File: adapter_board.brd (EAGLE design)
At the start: 40 x 40 mm, 29 parts, among them IC1 LT8336HV#PBF, J1 62684-401100AHLF, J2 SFV6R-3STE1HLF, J3 54548-2271

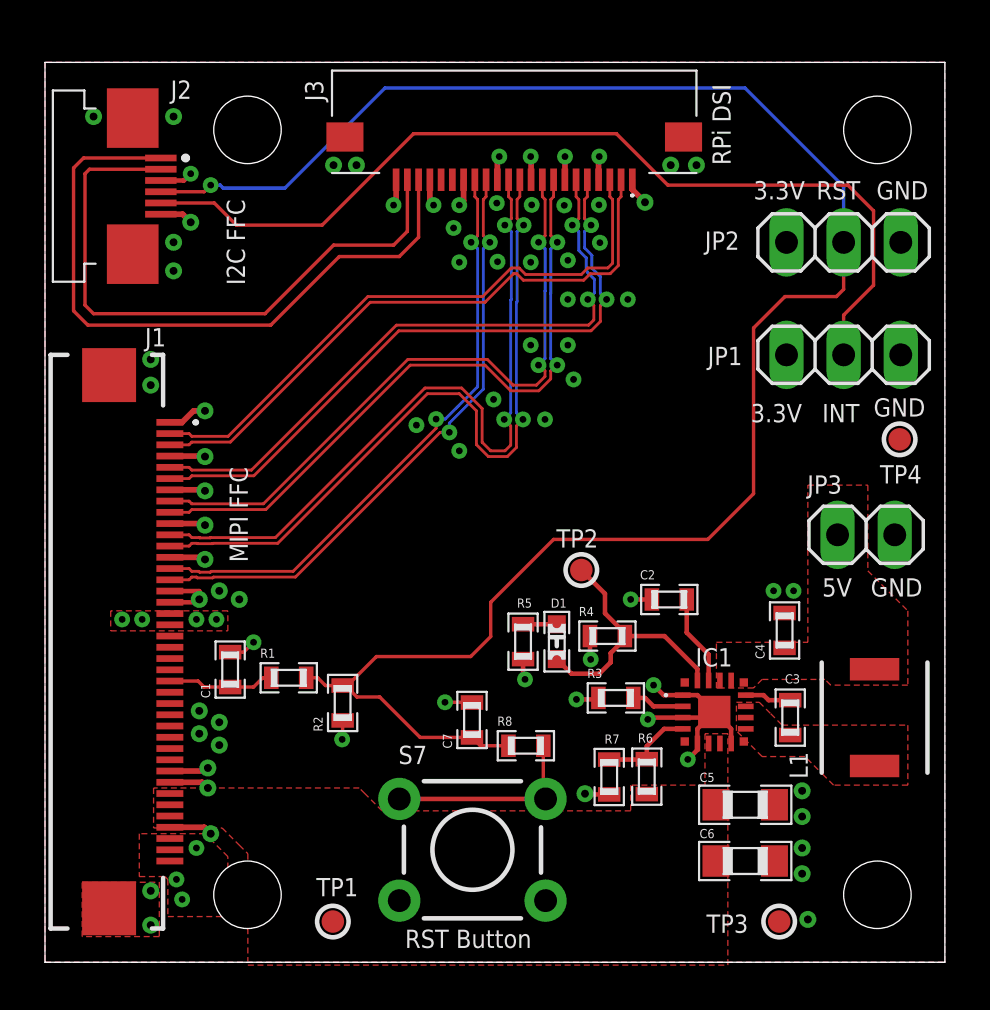
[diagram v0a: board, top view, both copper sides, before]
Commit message: Changed inductor L1.
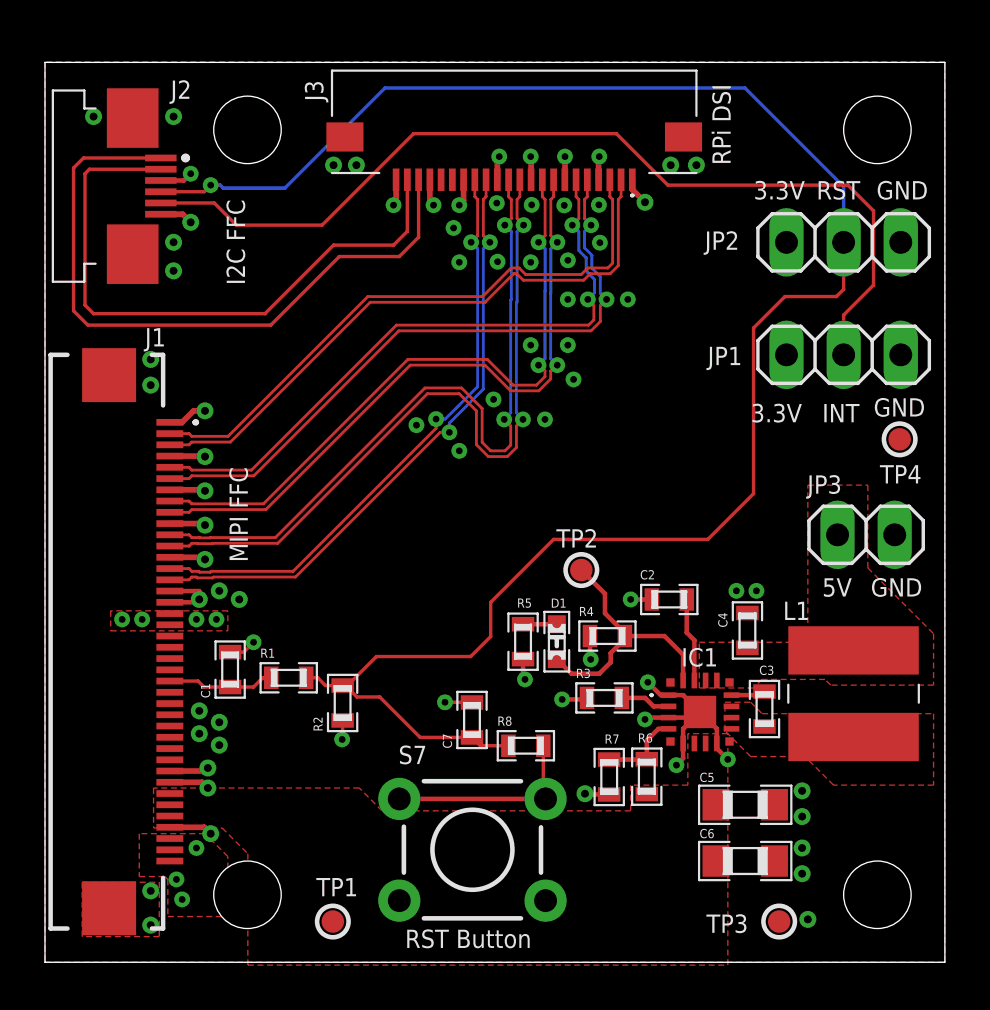
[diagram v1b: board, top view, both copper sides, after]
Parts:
- L1: value 1235AS-H-2R4M=P3 -> SDR0603-2R5ML; device SamacSys_Parts:1235ASH100MP3 -> SamacSys_Parts:SDR06032R5ML
- moved C4 1.65 mm to (31.2, 14.8)
- moved L1 1.42 mm to (35.9, 11.9), turned to 0 degrees
- moved C3 1.20 mm to (32.0, 11.3)
- moved IC1 0.64 mm to (29.1, 11.1)
- moved R3 0.51 mm to (24.9, 11.8)
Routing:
- net N$7: track 2.07 -> 1.53 mm
- net VSS: track 42.1 -> 42.5 mm, vias 69 -> 70

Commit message: Changed min width/spacing to 6/6. Length matched DSI traces.
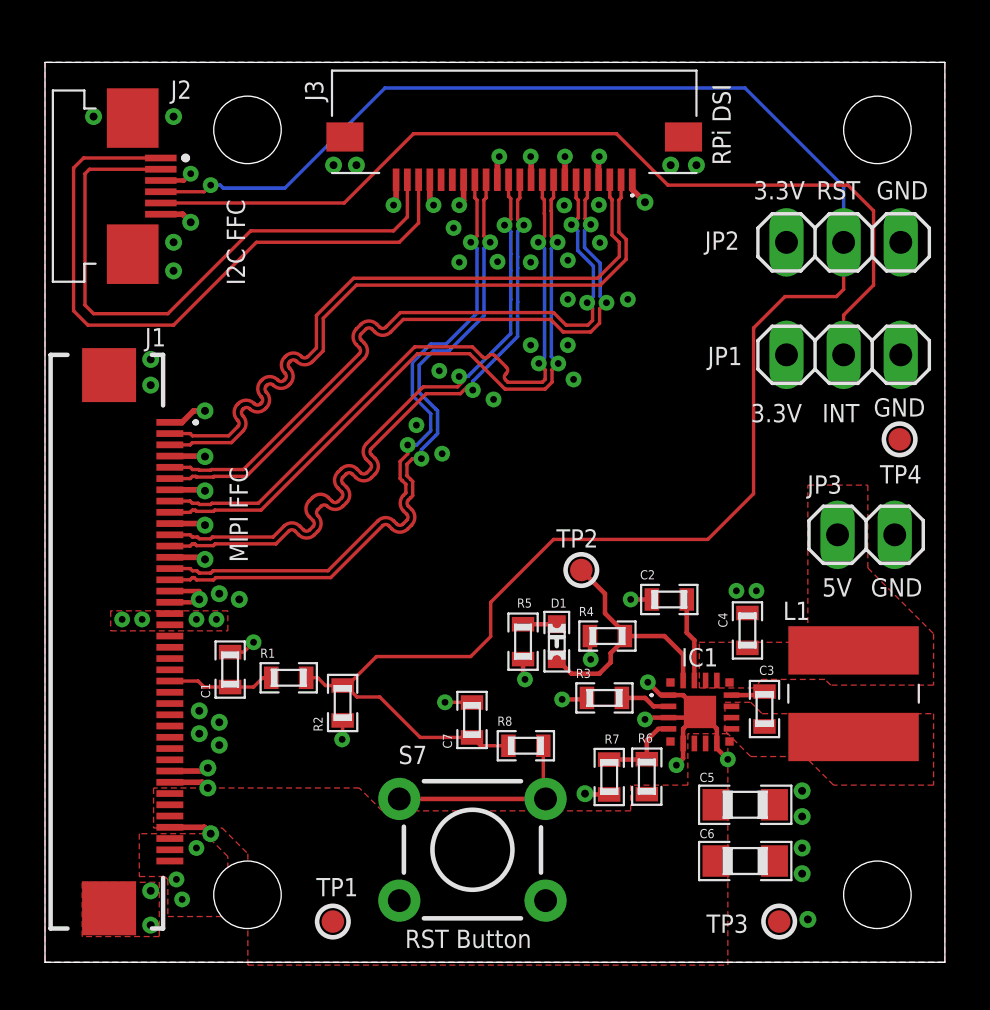
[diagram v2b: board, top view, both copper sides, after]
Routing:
- net DSI_D2_N: track 32.9 -> 29.6 mm
- net DSI_D3_N: track 27.3 -> 30.5 mm
- net DSI_D3_P: track 26.9 -> 30.0 mm
- net DSI_D2_P: track 32.5 -> 29.6 mm
- net DSI_D0_P: track 26.9 -> 29.6 mm
- net DSI_D0_N: track 27.3 -> 30.0 mm
- net DSI_D1_N: track 29.1 -> 30.6 mm
- net DSI_D1_P: track 28.7 -> 30.0 mm
- net DSI_CLK_P: track 29.3 -> 30.1 mm
- net !INT: track 42.1 -> 41.3 mm
- net DSI_CLK_N: track 29.7 -> 30.3 mm
- net VSS: vias 70 -> 68

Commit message: Changed PGOOD LED to 5V rail.
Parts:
- D1: value Red -> Green
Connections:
- net VCC_3V3: no longer R4.1, R5.2
- net VCC_5V0: now also R4.1, R5.2
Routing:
- net VCC_5V0: track 0.00 -> 14.8 mm, vias 0 -> 3
- net VCC_3V3: track 5.47 -> 3.48 mm, vias 12 -> 10
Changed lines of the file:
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@@
 <grid distance="5" unitdist="mil" unit="mil" style="dots" multiple="1" display="yes" altdistance="0.000123031496" altunitdist="mil" altunit="mil"/>
 <layers>
-<layer number="1" name="Top" color="4" fill="1" visible="no" active="yes"/>
-<layer number="2" name="Route2" color="16" fill="1" visible="no" active="yes"/>
+<layer number="1" name="Top" color="4" fill="1" visible="yes" active="yes"/>
+<layer number="2" name="Route2" color="16" fill="1" visible="yes" active="yes"/>
 <layer number="3" name="Route3" color="17" fill="1" visible="no" active="no"/>
 <layer number="4" name="Route4" color="18" fill="1" visible="no" active="no"/>
@@
 <layer number="13" name="Route13" color="21" fill="1" visible="no" active="no"/>
 <layer number="14" name="Route14" color="22" fill="1" visible="no" active="no"/>
-<layer number="15" name="Route15" color="23" fill="1" visible="no" active="yes"/>
+<layer number="15" name="Route15" color="23" fill="1" visible="yes" active="yes"/>
 <layer number="16" name="Bottom" color="1" fill="1" visible="yes" active="yes"/>
 <layer number="17" name="Pads" color="2" fill="1" visible="yes" active="yes"/>
@@
 <layer number="19" name="Unrouted" color="6" fill="1" visible="no" active="yes"/>
 <layer number="20" name="Dimension" color="24" fill="1" visible="yes" active="yes"/>
-<layer number="21" name="tPlace" color="7" fill="1" visible="no" active="yes"/>
+<layer number="21" name="tPlace" color="7" fill="1" visible="yes" active="yes"/>
 <layer number="22" name="bPlace" color="7" fill="1" visible="yes" active="yes"/>
-<layer number="23" name="tOrigins" color="15" fill="1" visible="no" active="yes"/>
+<layer number="23" name="tOrigins" color="15" fill="1" visible="yes" active="yes"/>
 <layer number="24" name="bOrigins" color="15" fill="1" visible="yes" active="yes"/>
-<layer number="25" name="tNames" color="7" fill="1" visible="no" active="yes"/>
+<layer number="25" name="tNames" color="7" fill="1" visible="yes" active="yes"/>
 <layer number="26" name="bNames" color="7" fill="1" visible="yes" active="yes"/>
-<layer number="27" name="tValues" color="7" fill="1" visible="no" active="yes"/>
+<layer number="27" name="tValues" color="7" fill="1" visible="yes" active="yes"/>
 <layer number="28" name="bValues" color="7" fill="1" visible="yes" active="yes"/>
 <layer number="29" name="tStop" color="7" fill="3" visible="no" active="yes"/>
@@
 <attribute name="VALUE" x="20.25" y="9.5" size="0.4064" layer="27" font="vector" rot="R90" display="off"/>
 </element>
-<element name="D1" library="standardparts" package="0603.LED" value="Red" x="22.75" y="14.25" smashed="yes" rot="R270">
+<element name="D1" library="standardparts" package="0603.LED" value="Green" x="22.75" y="14.25" smashed="yes" rot="R270">
 <attribute name="NAME" x="22.48" y="15.762" size="0.4064" layer="25" font="vector"/>
 <attribute name="VALUE" x="21.607" y="15.52" size="0.4064" layer="27" font="vector" rot="R270" display="off"/>
@@
 <contactref element="JP1" pad="1"/>
 <contactref element="JP2" pad="1"/>
-<contactref element="R4" pad="1"/>
-<contactref element="R5" pad="2"/>
 <wire x1="15.607" y1="34.784" x2="15.607" y2="33.768" width="0.254" layer="1"/>
 <wire x1="15.607" y1="33.768" x2="15.494" y2="33.655" width="0.254" layer="1"/>
@@
 <wire x1="13.23" y1="9.928" x2="13.208" y2="9.906" width="0.1524" layer="1"/>
 <via x="13.208" y="9.906" extent="1-16" drill="0.3"/>
-<wire x1="24.225" y1="14.5" x2="24.225" y2="13.494" width="0.2032" layer="1"/>
-<wire x1="24.225" y1="13.494" x2="24.257" y2="13.462" width="0.2032" layer="1"/>
-<via x="24.257" y="13.462" extent="1-16" drill="0.3"/>
-<wire x1="21.25" y1="13.475" x2="21.25" y2="12.659" width="0.2032" layer="1"/>
-<wire x1="21.25" y1="12.659" x2="21.336" y2="12.573" width="0.2032" layer="1"/>
-<via x="21.336" y="12.573" extent="1-16" drill="0.3"/>
 <via x="6.731" y="5.08" extent="1-16" drill="0.3"/>
 <via x="5.842" y="3.683" extent="1-16" drill="0.3"/>
@@
 </polygon>
 <contactref element="L1" pad="2"/>
+<contactref element="R4" pad="1"/>
+<contactref element="R5" pad="2"/>
+<wire x1="24.225" y1="14.5" x2="24.225" y2="13.494" width="0.2032" layer="1"/>
+<wire x1="24.225" y1="13.494" x2="24.257" y2="13.462" width="0.2032" layer="1"/>
+<via x="24.257" y="13.462" extent="1-16" drill="0.3"/>
+<wire x1="21.25" y1="13.475" x2="21.25" y2="12.659" width="0.2032" layer="1"/>
+<wire x1="21.25" y1="12.659" x2="21.336" y2="12.573" width="0.2032" layer="1"/>
+<via x="21.336" y="12.573" extent="1-16" drill="0.3"/>
+<wire x1="21.336" y1="12.573" x2="22.225" y2="13.462" width="0.254" layer="16"/>
+<wire x1="22.225" y1="13.462" x2="24.257" y2="13.462" width="0.254" layer="16"/>
+<wire x1="24.257" y1="13.462" x2="25.146" y2="13.462" width="0.254" layer="16"/>
+<wire x1="32.639" y1="14.097" x2="33.274" y2="13.462" width="0.254" layer="16"/>
+<via x="33.274" y="13.462" extent="1-16" drill="0.35"/>
+<wire x1="25.146" y1="13.462" x2="25.781" y2="14.097" width="0.254" layer="16"/>
+<wire x1="25.781" y1="14.097" x2="32.639" y2="14.097" width="0.254" layer="16"/>
 </signal>
 <signal name="N$7">

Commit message: Changed D1 back to red.
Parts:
- D1: value Green -> Red
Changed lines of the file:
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@@
 <attribute name="VALUE" x="20.25" y="9.5" size="0.4064" layer="27" font="vector" rot="R90" display="off"/>
 </element>
-<element name="D1" library="standardparts" package="0603.LED" value="Green" x="22.75" y="14.25" smashed="yes" rot="R270">
+<element name="D1" library="standardparts" package="0603.LED" value="Red" x="22.75" y="14.25" smashed="yes" rot="R270">
 <attribute name="NAME" x="22.48" y="15.762" size="0.4064" layer="25" font="vector"/>
 <attribute name="VALUE" x="21.607" y="15.52" size="0.4064" layer="27" font="vector" rot="R270" display="off"/>
